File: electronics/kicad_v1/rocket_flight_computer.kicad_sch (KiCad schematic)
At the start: 10 parts, among them U1 BMP390, U2 Teensy4.1, U3 BMI088, U4 NEO-M8N

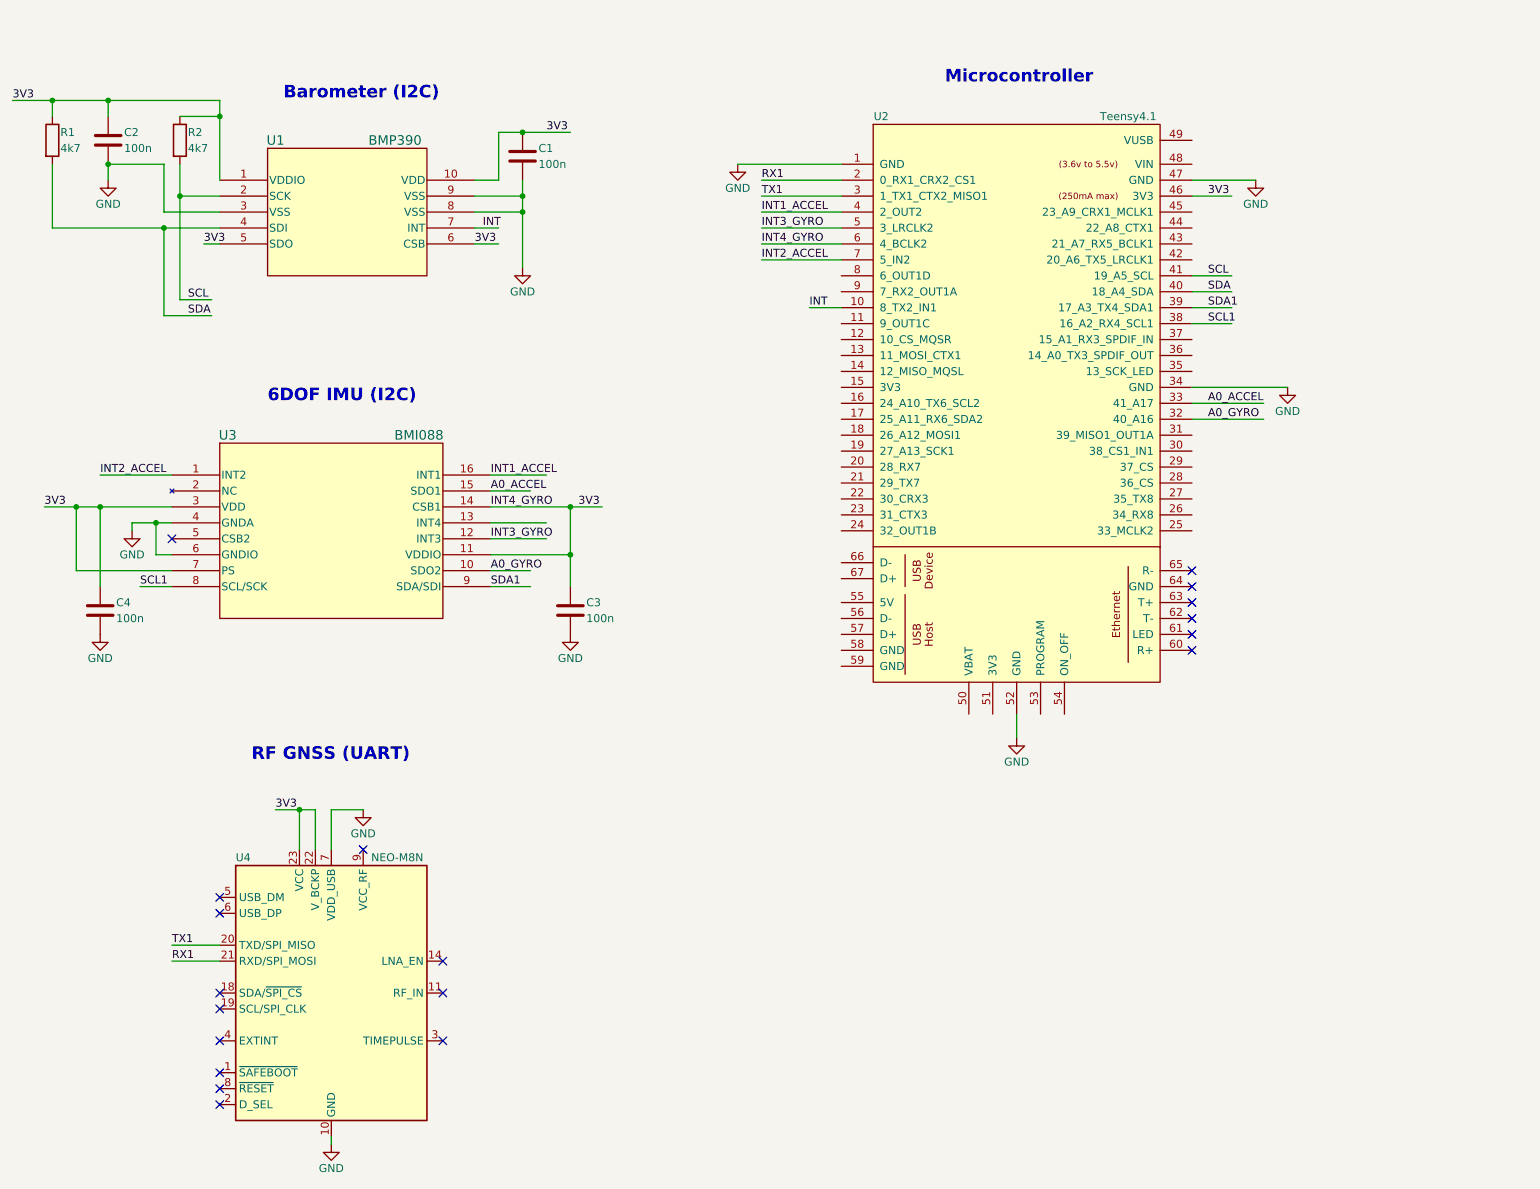
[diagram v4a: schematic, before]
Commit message: all components in the same libary, add gps
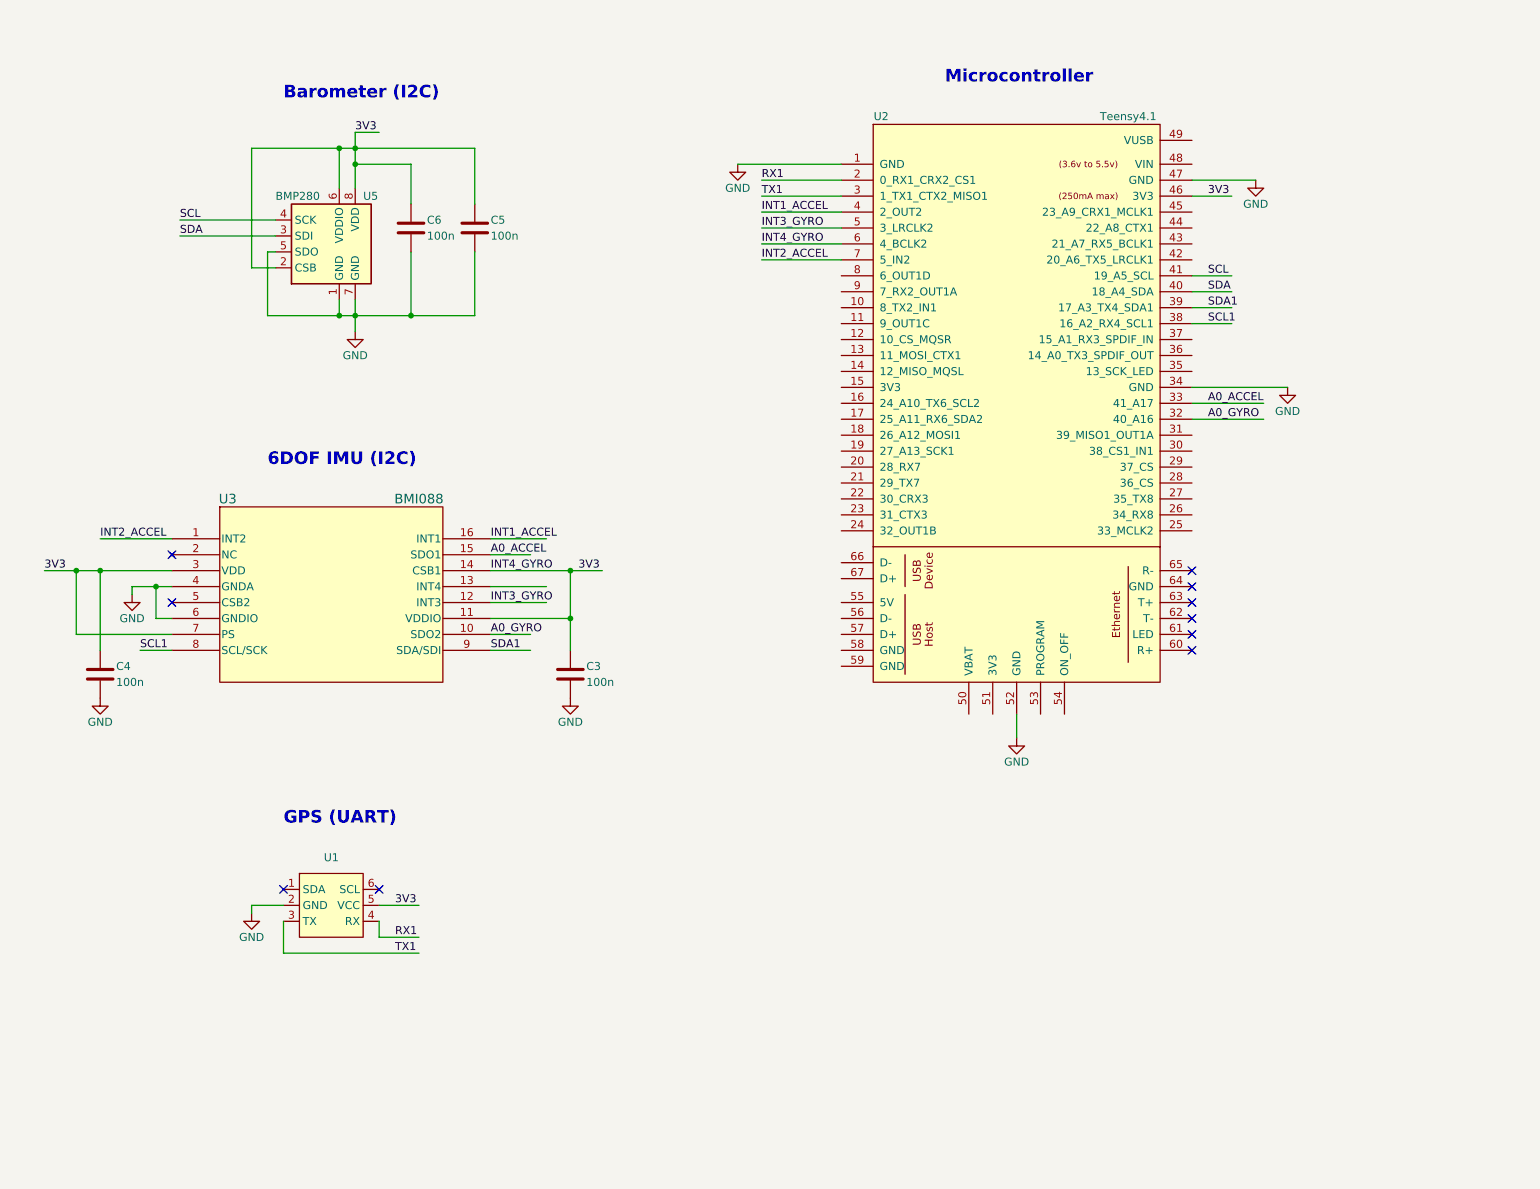
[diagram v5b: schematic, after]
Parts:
- removed C1, C2: 100n, symbol Device:C
- removed R1, R2: 4k7, symbol Device:R
- removed U1: BMP390, LGA10_BMP390_BOS, symbol bmp390:BMP390
- removed U2: Teensy4.1, symbol teensy:Teensy4.1
- removed U3: BMI088, QFN_BMI085_BOS, symbol BMI088:BMI088
- removed U4: NEO-M8N, RF_GPS:ublox_NEO, symbol RF_GPS:NEO-M8N
- added C5, C6: 100n, symbol Device:C
- added U1: ~, symbol components:BN-880
- added U2: Teensy4.1, symbol components:Teensy4.1
- added U3: BMI088, QFN_BMI085_BOS, symbol components:BMI088
- added U5: BMP280, Package_LGA:Bosch_LGA-8_2x2.5mm_P0.65mm_ClockwisePinNumbering, symbol Sensor_Pressure:BMP280
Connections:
- net 3V3: now also C5.1, C6.1, U1.5 (VCC), U2.46 (3V3), U2.6 (4_BCLK2), U3.11 (VDDIO), U3.14 (CSB1), U3.3 (VDD), U3.7 (PS), U5.2 (CSB), U5.6 (VDDIO), U5.8 (VDD)
- net A0_ACCEL: now also U2.33 (41_A17), U3.15 (SDO1)
- net A0_GYRO: now also U2.32 (40_A16), U3.10 (SDO2)
- net GND: now also C5.2, C6.2, U1.2 (GND), U2.1 (GND), U2.34 (GND), U2.47 (GND), U2.52 (GND), U3.4 (GNDA), U3.6 (GNDIO), U5.1 (GND), U5.5 (SDO), U5.7 (GND)
- net INT1_ACCEL: now also U2.4 (2_OUT2), U3.16 (INT1)
- net INT2_ACCEL: now also U2.7 (5_IN2), U3.1 (INT2)
- net INT3_GYRO: now also U2.5 (3_LRCLK2), U3.12 (INT3)
- net RX1: now also U1.4 (RX), U2.2 (0_RX1_CRX2_CS1)
- net SCL: now also U2.41 (19_A5_SCL), U5.4 (SCK)
- net SCL1: now also U2.38 (16_A2_RX4_SCL1), U3.8 (SCL/SCK)
- net SDA: now also U2.40 (18_A4_SDA), U5.3 (SDI)
- net SDA1: now also U2.39 (17_A3_TX4_SDA1), U3.9 (SDA/SDI)
- net TX1: now also U1.3 (TX), U2.3 (1_TX1_CTX2_MISO1)
- no-connect marks 19 -> 10
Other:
- note added: "GPS (UART)"
- note removed: "RF GNSS (UART)"
- moved on the sheet: C3, C4
